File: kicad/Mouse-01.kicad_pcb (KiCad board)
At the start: 2 copper layers, 74 x 72 mm, 91 parts, among them P1 MT-ENC, P2 MT-ENC, P3 Battery_A, P4 Battery_B, P5 SWD, P6 UART, Q1 IRFML8244, Q2 IRFML8244, Q3 BSS138, SW1 RESET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

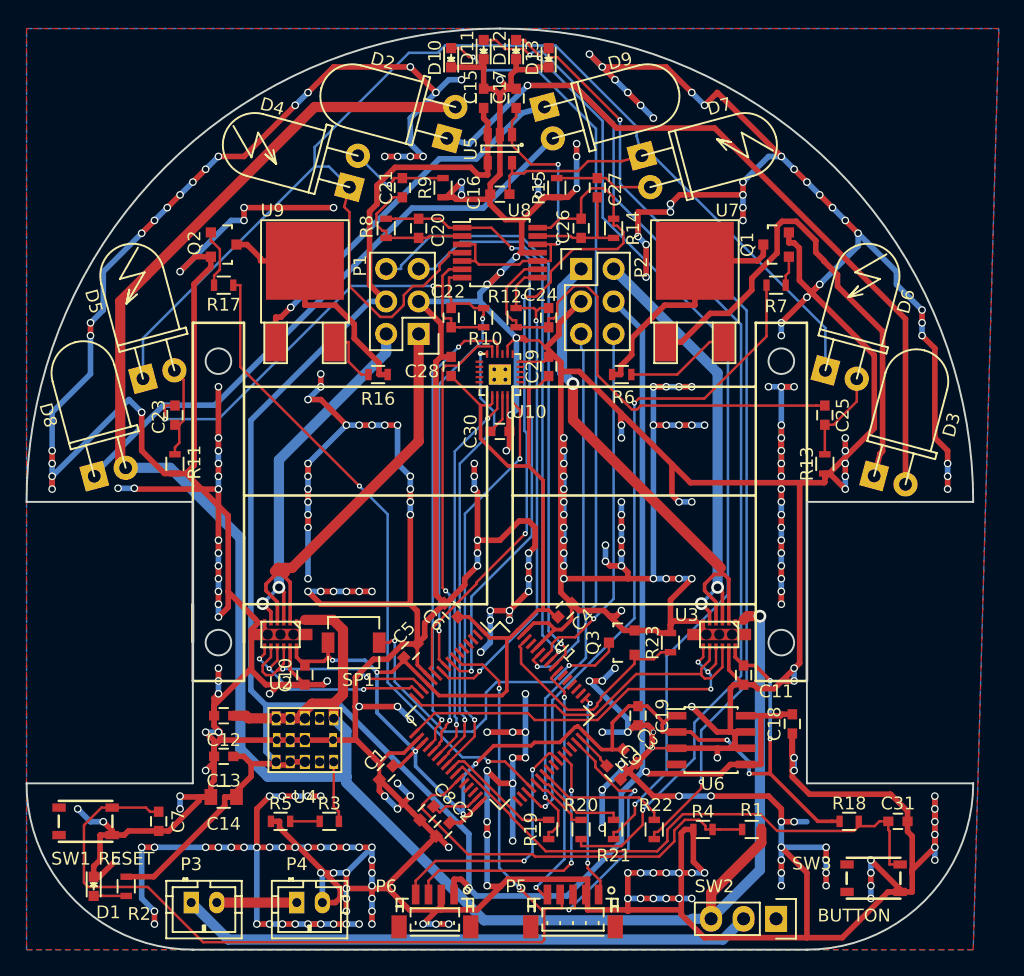
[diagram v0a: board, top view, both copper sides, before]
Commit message: 左右のスラローム実装
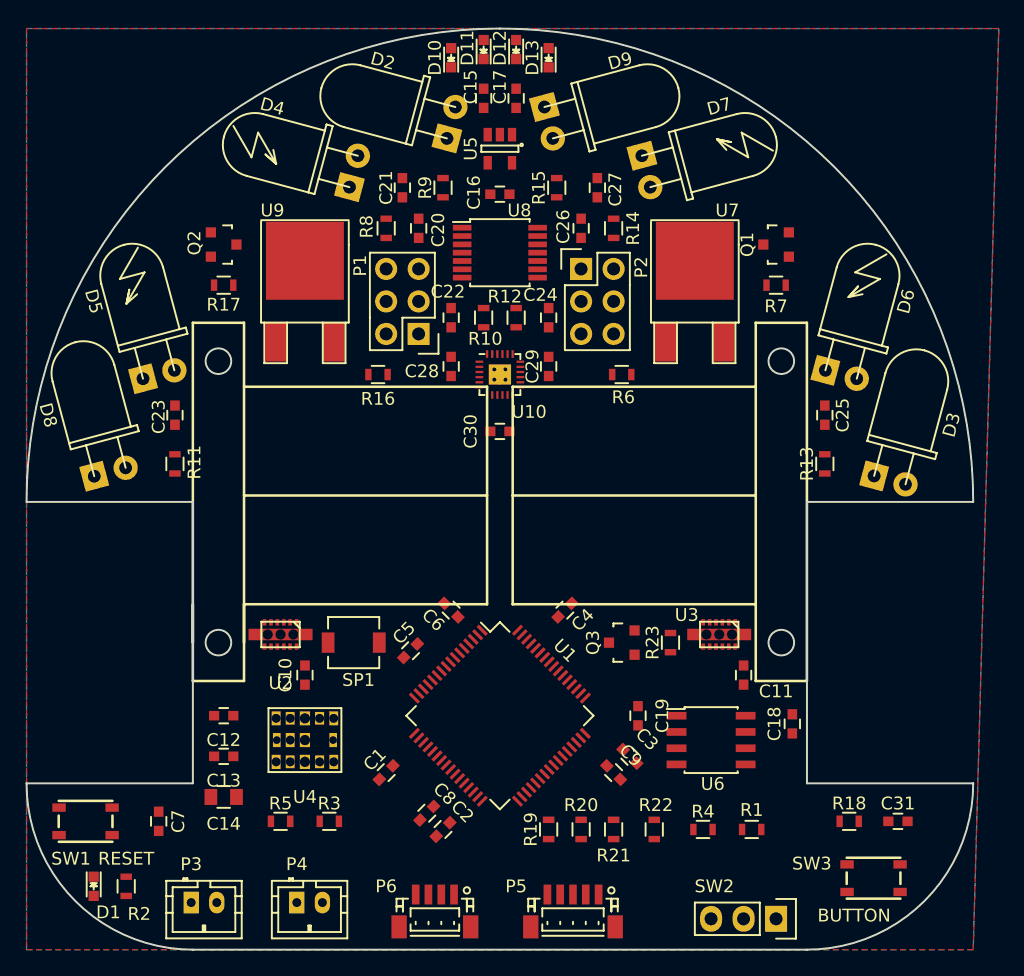
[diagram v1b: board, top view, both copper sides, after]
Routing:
- net GND: track 1097.5 -> 0.00 mm, vias 322 -> 0
- net +5V: track 189.7 -> 0.00 mm, vias 2 -> 0
- net +BATT: track 177.5 -> 0.00 mm, vias 1 -> 0
- net +3V3: track 145.8 -> 0.00 mm, vias 9 -> 0
- net +3.3VADC: track 117.5 -> 0.00 mm
- net Net-(D11-Pad2): track 81.3 -> 0.00 mm, vias 2 -> 0
- net RESET: track 77.6 -> 0.00 mm, vias 2 -> 0
- net Net-(D12-Pad2): track 73.6 -> 0.00 mm, vias 2 -> 0
- net Net-(D10-Pad2): track 72.0 -> 0.00 mm, vias 2 -> 0
- net Net-(D13-Pad2): track 71.8 -> 0.00 mm, vias 2 -> 0
- net /IR_LED_SL_FR/IR_LED_1: track 58.3 -> 0.00 mm, vias 1 -> 0
- net PR-RCV-SR: track 55.6 -> 0.00 mm, vias 2 -> 0
- net PR-LED-SL-FR: track 52.8 -> 0.00 mm, vias 2 -> 0
- net PR-LED-FL_SR: track 51.0 -> 0.00 mm, vias 2 -> 0
- net PR-RCV-SL: track 48.7 -> 0.00 mm, vias 2 -> 0
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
